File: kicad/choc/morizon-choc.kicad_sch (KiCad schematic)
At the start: 145 parts

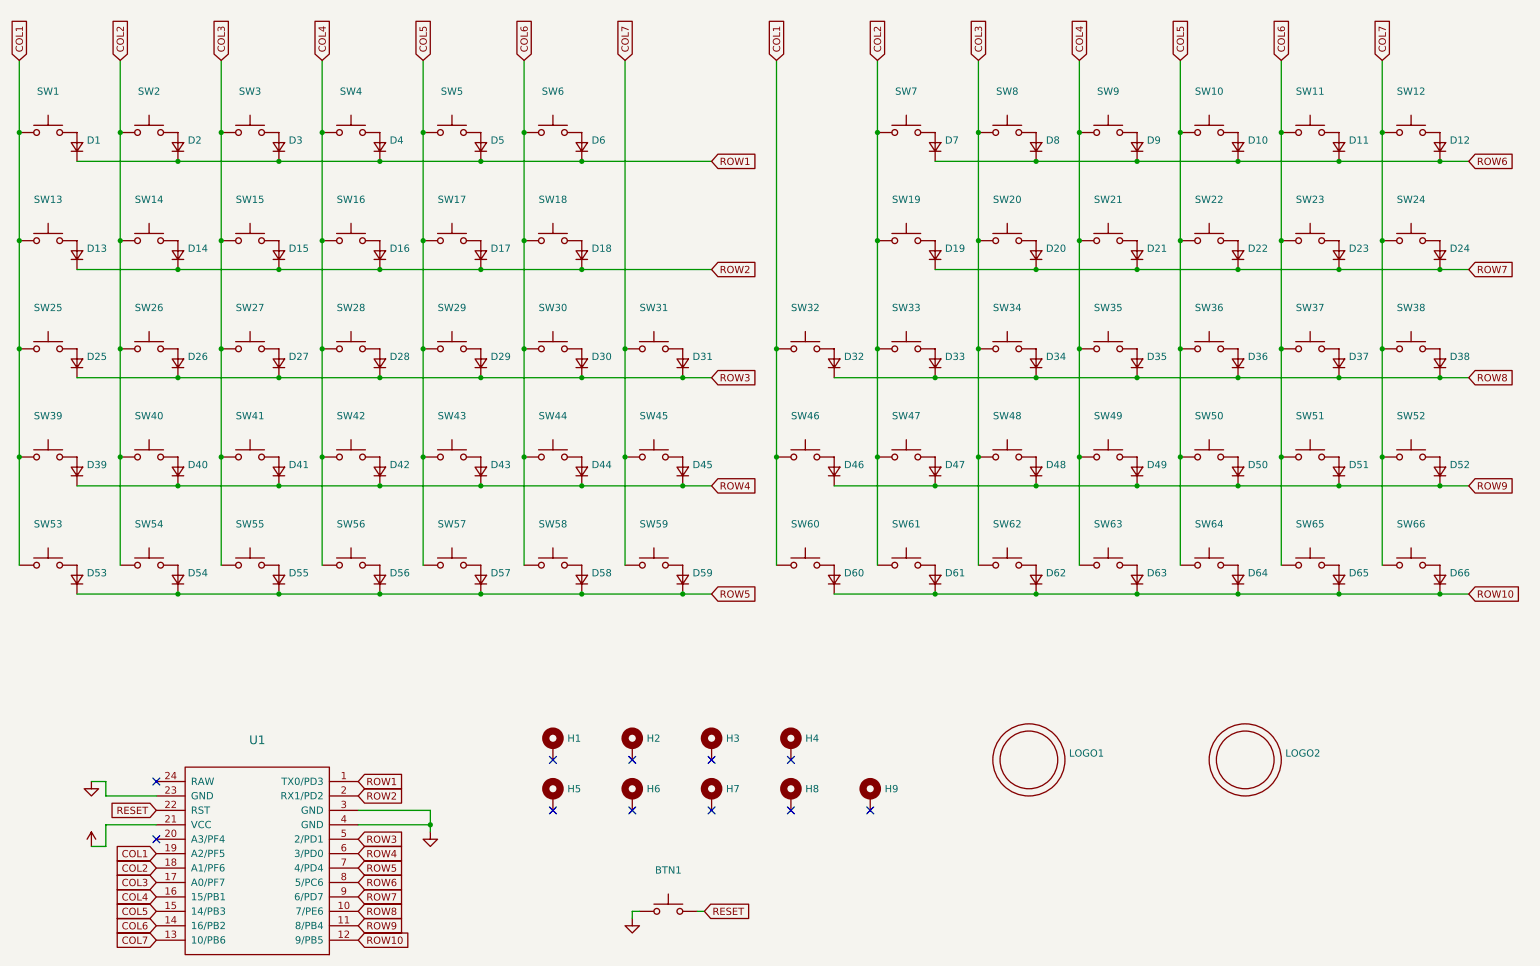
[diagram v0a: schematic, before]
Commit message: Use KiCad 6 symbol library format
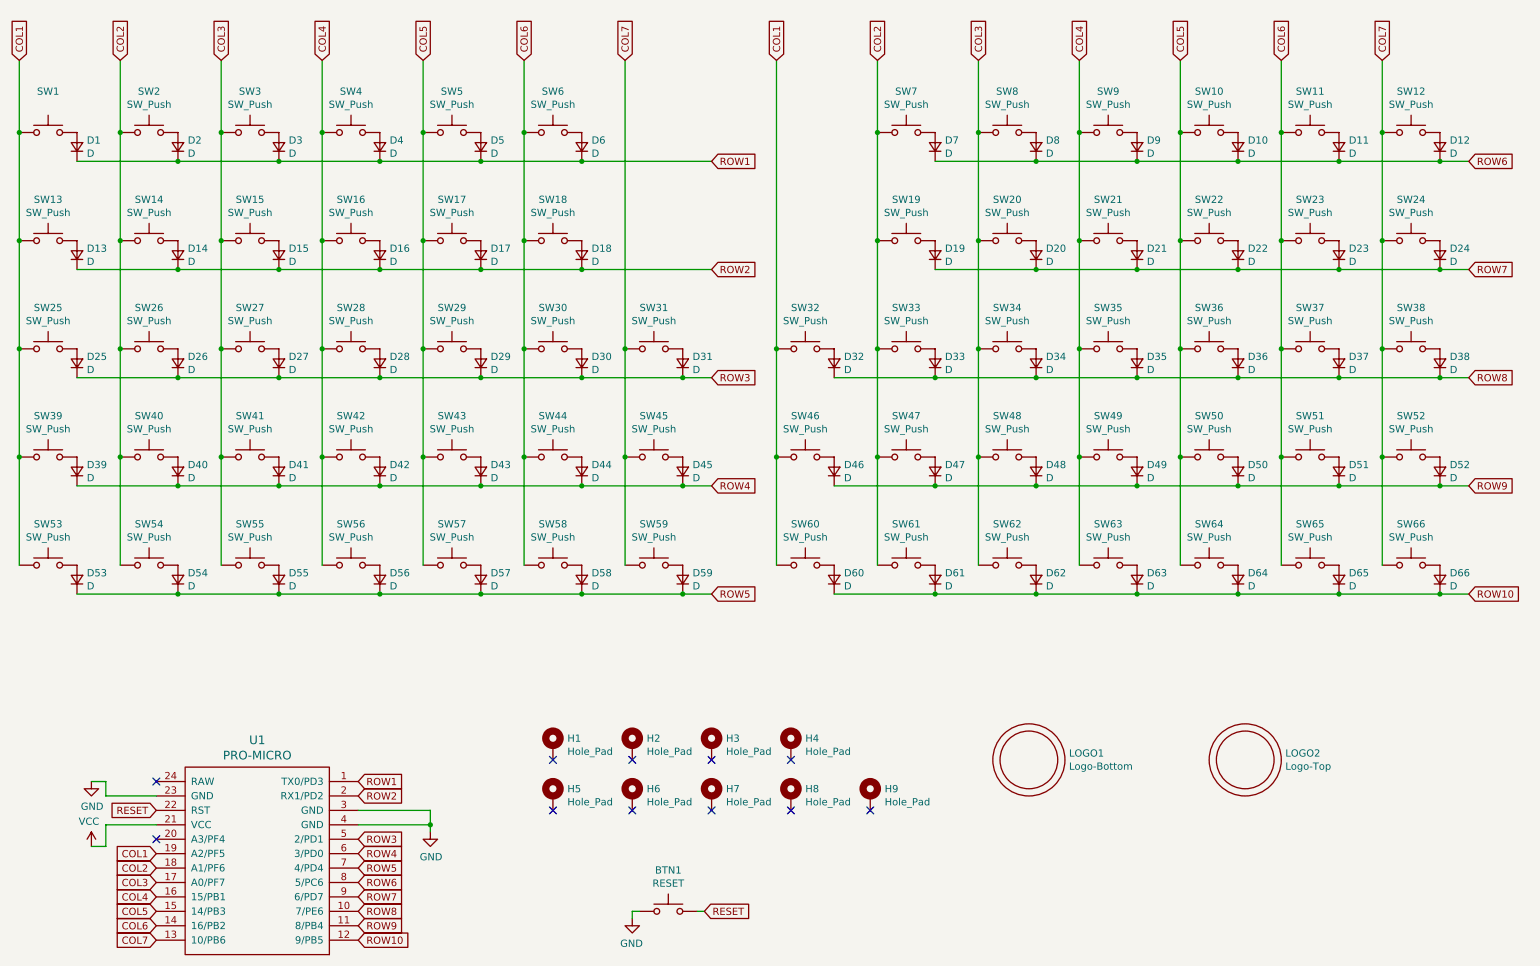
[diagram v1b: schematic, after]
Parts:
- BTN1: value (none) -> RESET; footprint (none) -> horizon-footprints:SW_Push_6mm
- D1, D10, D11, D12, D13, D14, D15, D16, D17, D18, D19, D2, D20, D21, D22, D23, D24, D25, D26, D27, D28, D29, D3, D30, D31, D32, D33, D34, D35, D36, D37, D38, D39, D4, D40, D41, D42, D43, D44, D45, D46, D47, D48, D49, D5, D50, D51, D52, D53, D54, D55, D56, D57, D58, D59, D6, D60, D61, D62, D63, D64, D65, D66, D7, D8, D9: value (none) -> D; footprint (none) -> horizon-footprints:D_SOD-123
- H1, H2, H3, H4, H5, H6, H7, H8, H9: value (none) -> Hole_Pad; footprint (none) -> horizon-footprints:Mount_M2
- LOGO1: value (none) -> Logo-Bottom; footprint (none) -> horizon-footprints:Logo_Morizon_Small
- LOGO2: value (none) -> Logo-Top; footprint (none) -> horizon-footprints:Logo_Morizon_M
- SW10, SW11, SW12, SW13, SW14, SW15, SW16, SW17, SW18, SW19, SW2, SW20, SW21, SW22, SW23, SW24, SW25, SW26, SW27, SW28, SW29, SW3, SW30, SW31, SW32, SW33, SW34, SW35, SW36, SW37, SW38, SW39, SW4, SW40, SW41, SW42, SW43, SW44, SW45, SW46, SW47, SW48, SW49, SW5, SW50, SW51, SW52, SW53, SW54, SW55, SW56, SW57, SW58, SW59, SW6, SW60, SW61, SW62, SW63, SW64, SW65, SW66, SW7, SW8, SW9: value (none) -> SW_Push; footprint (none) -> horizon-footprints:SW_Choc
- U1: value (none) -> PRO-MICRO; footprint (none) -> horizon-footprints:Pro-Micro

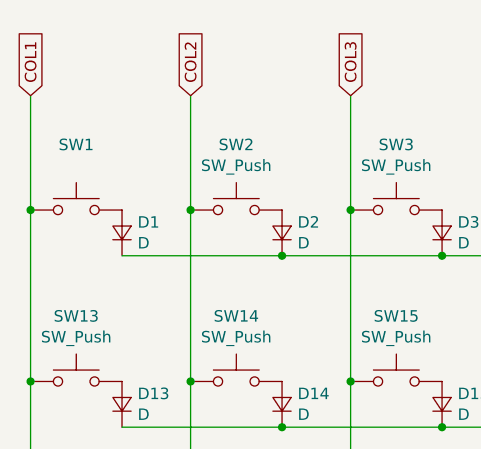
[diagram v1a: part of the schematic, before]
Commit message: Upgrade project files to KiCad 7
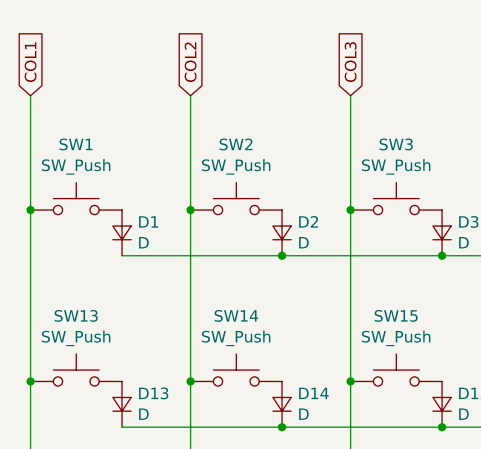
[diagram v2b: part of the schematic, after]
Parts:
- SW1: value (none) -> SW_Push; footprint (none) -> horizon-footprints:SW_Choc
